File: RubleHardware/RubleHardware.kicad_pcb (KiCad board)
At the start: 4 copper layers, 63 x 43 mm, 50 parts, among them IC1 LTC3780EUH#PBF, J1_IN1 Conn_01x08_Male, J2_OUT1 Conn_01x08_Male

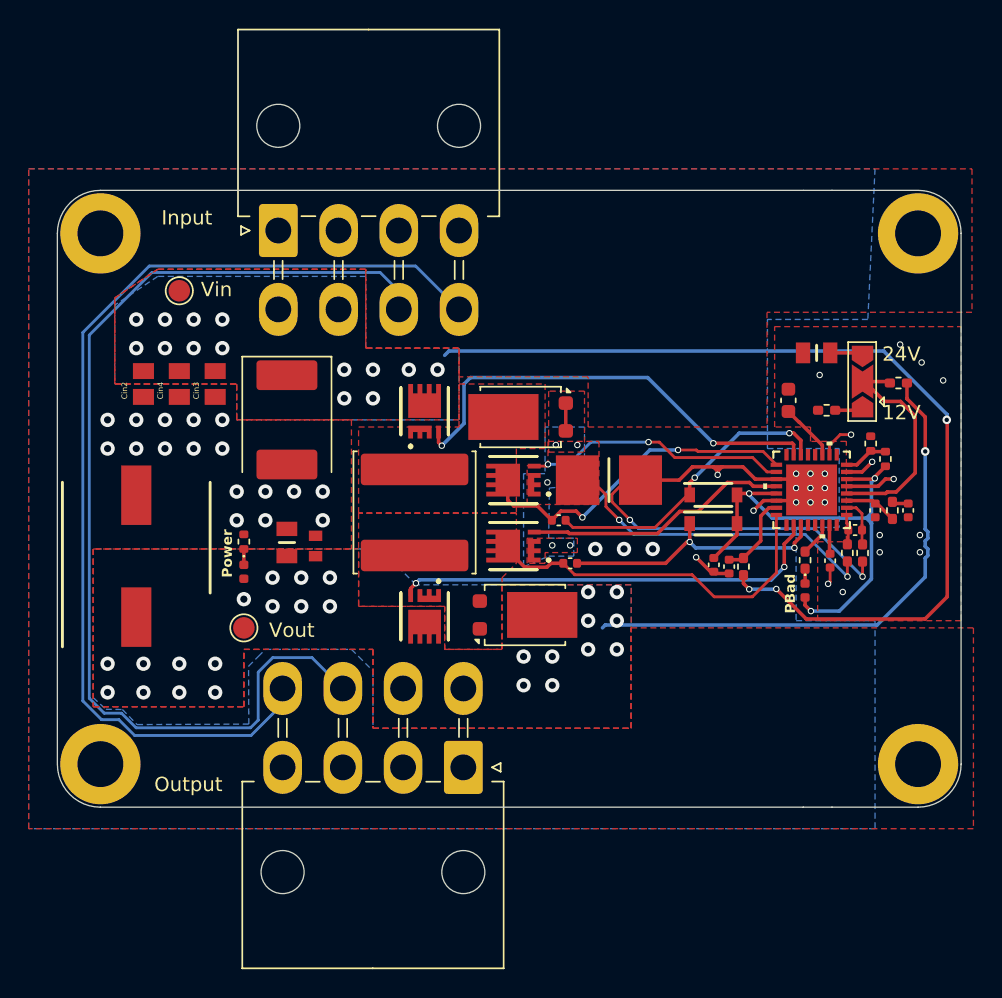
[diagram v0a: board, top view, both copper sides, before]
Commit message: Minor tweaks
Moved GND mounting holes away from edge
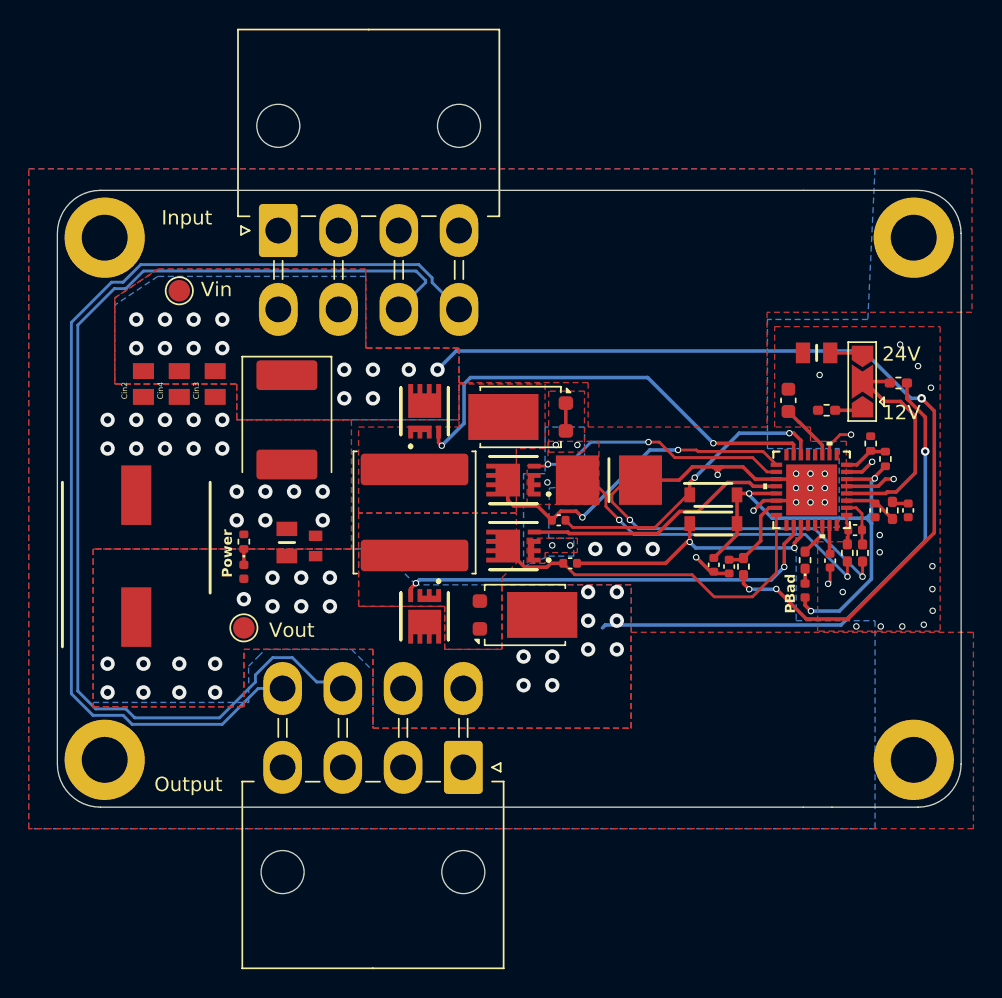
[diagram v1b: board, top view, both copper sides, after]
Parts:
- moved H1 0.42 mm to (136.3, 67.8)
- moved H2 0.42 mm to (136.3, 104.2)
- moved H3 0.42 mm to (192.7, 67.8)
- moved H4 0.42 mm to (192.7, 104.2)
- turned L1 to -90 degrees
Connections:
- L1 pad 1: /SW1 -> /SW2
- L1 pad 2: /SW2 -> /SW1
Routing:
- net /ICVIN: track 66.2 -> 62.8 mm
- net /CAN-: track 73.9 -> 76.6 mm
- net /ICVOUT: track 38.3 -> 36.5 mm
- net /CAN+: track 72.0 -> 72.7 mm
- net GND: vias 47 -> 52
